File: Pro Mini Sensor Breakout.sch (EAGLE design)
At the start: 15 parts, among them J1 22-27-2021-02, J10 22-27-2021-02, J11 22-27-2021-02, J12 22-27-2021-02, J2 22-27-2041-04, J3 22-27-2041-04, J4 22-27-2031-03, J5 22-27-2041-04, J6 22-27-2041-04, J7 22-27-2031-03, J8 22-27-2021-02, J9 22-27-2021-02, U1 ARDUINO_PRO_MINI

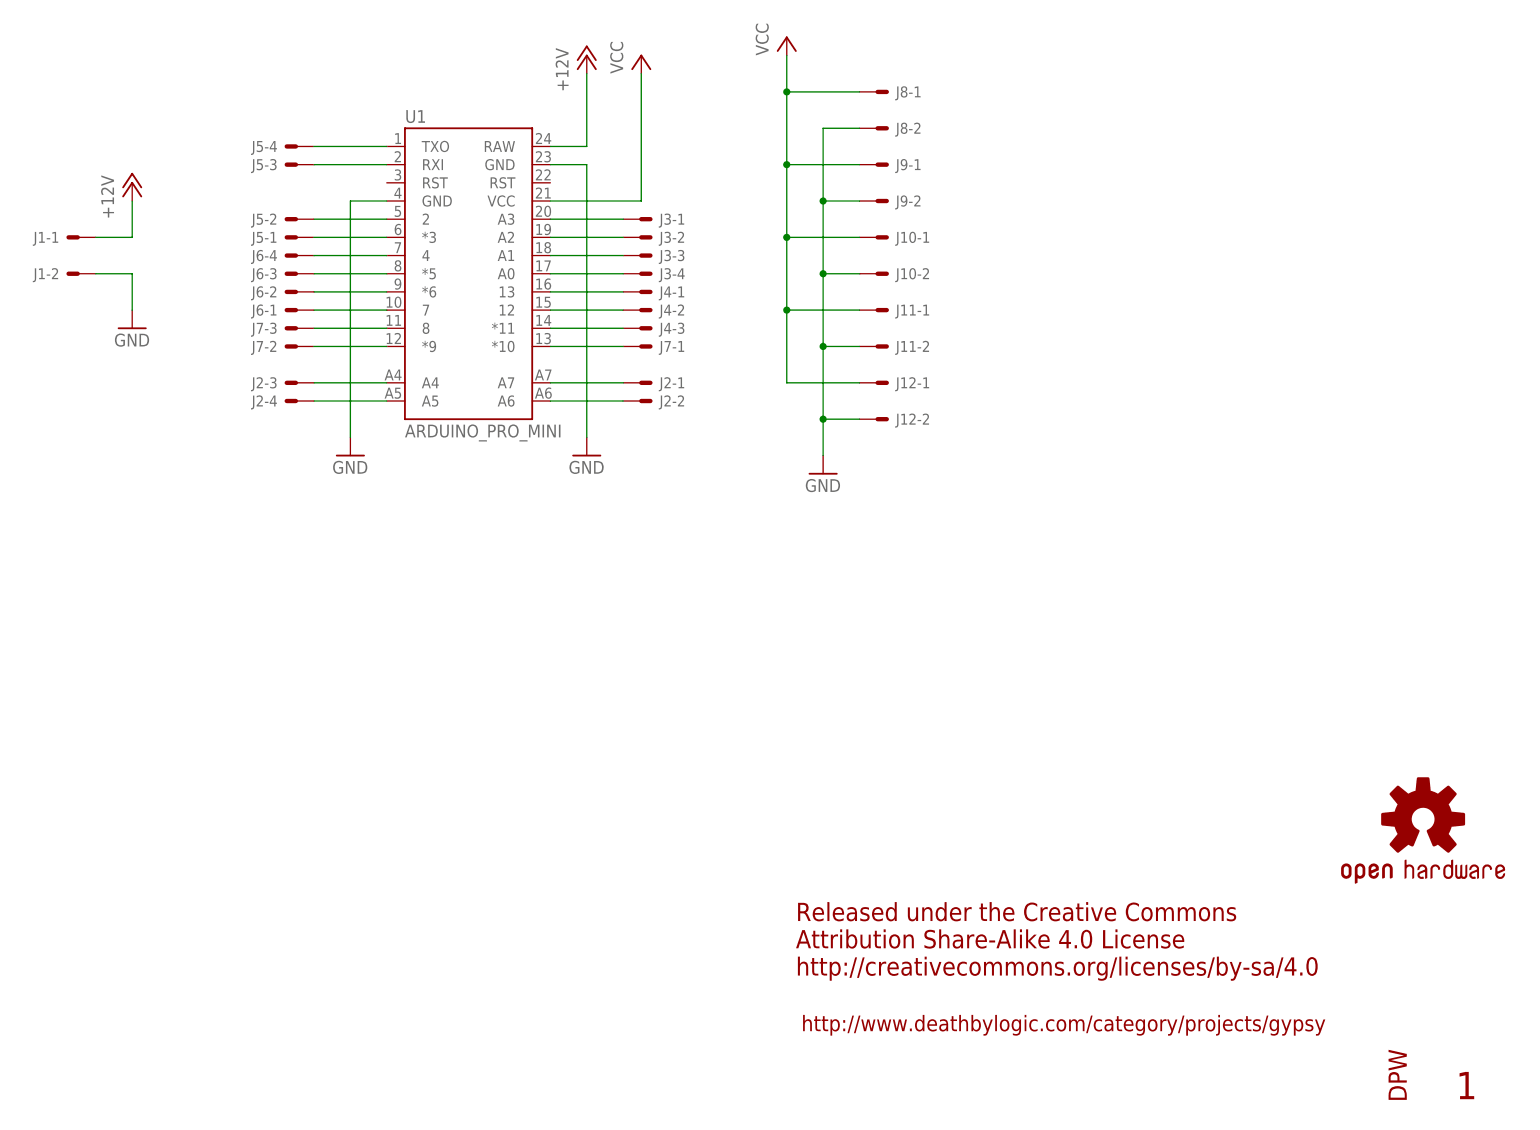
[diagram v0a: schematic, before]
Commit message: Corrected mis-wire of A4 & A5.
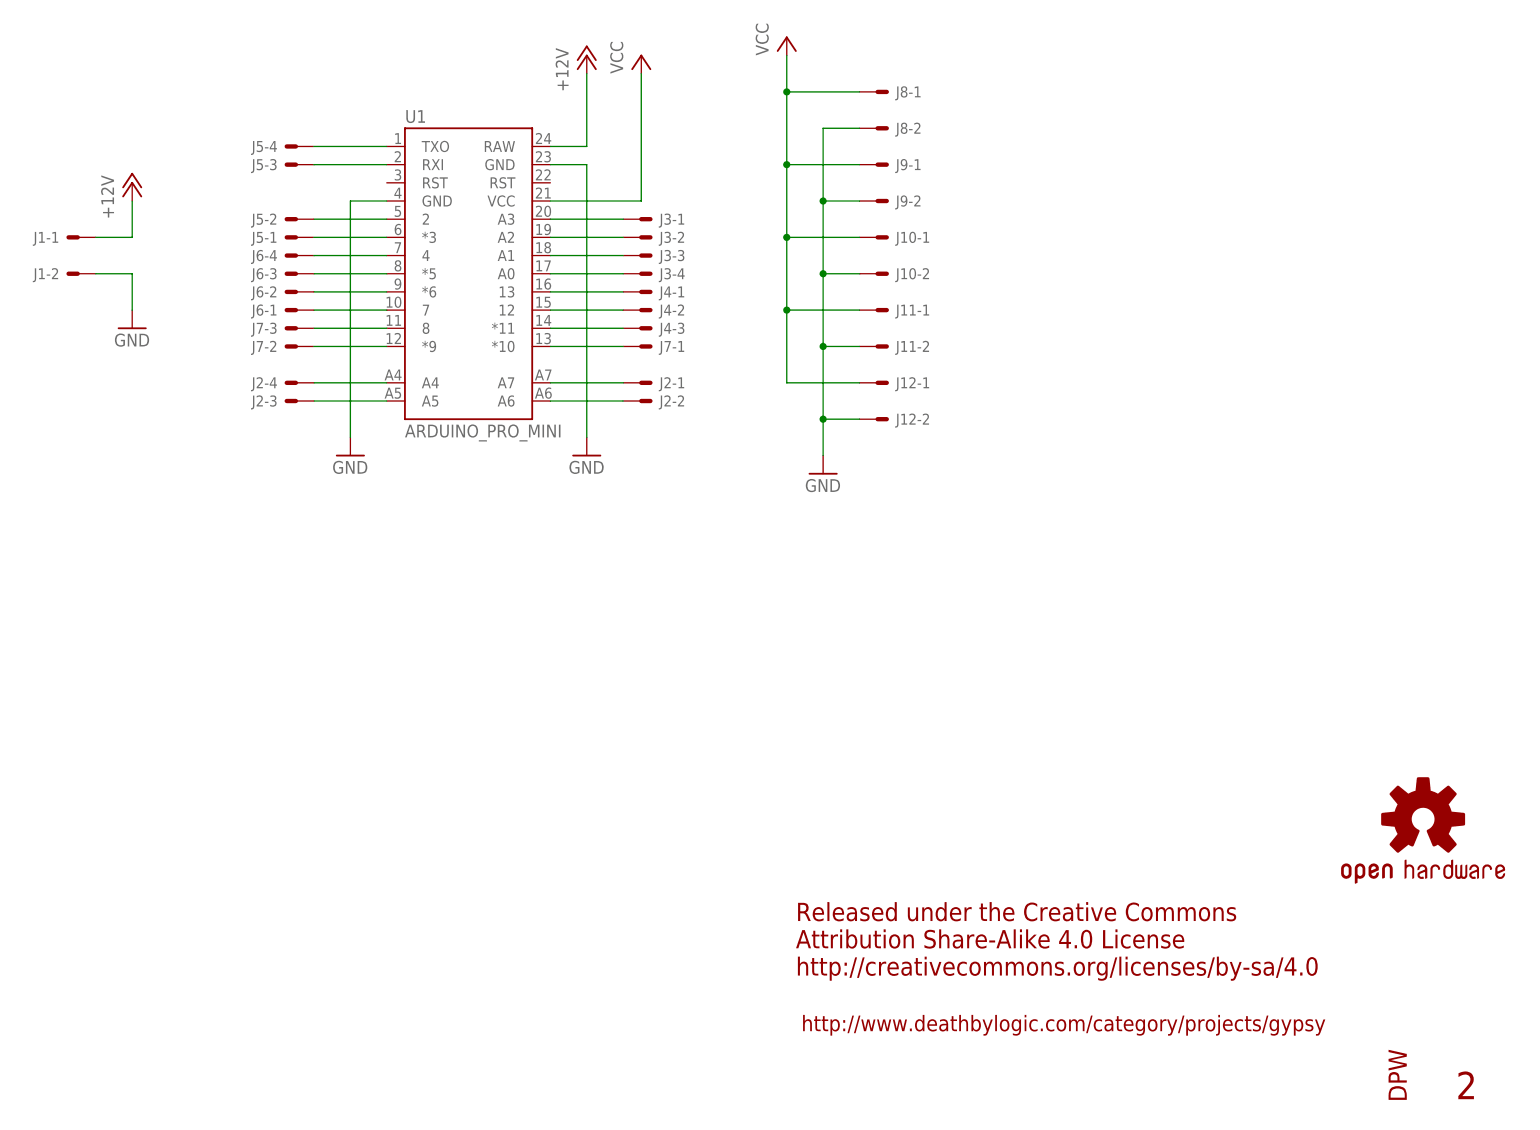
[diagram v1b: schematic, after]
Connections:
- removed net N$3: J2-4.S, U1.A5
- new net N$1: J2-4.S, U1.A4
- net N$2: now also U1.A5; no longer U1.A4
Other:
- note added: "2"
- note removed: "1"
- moved on the sheet: J2-3, J2-4
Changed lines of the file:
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@@
 <setting verticaltext="up"/>
 </settings>
-<grid distance="0.1" unitdist="inch" unit="inch" style="dots" multiple="1" display="yes" altdistance="0.01" altunitdist="inch" altunit="inch"/>
+<grid distance="0.1" unitdist="inch" unit="inch" style="lines" multiple="1" display="no" altdistance="0.01" altunitdist="inch" altunit="inch"/>
 <layers>
 <layer number="1" name="Top" color="4" fill="1" visible="no" active="no"/>
@@
 Attribution Share-Alike 4.0 License
 http://creativecommons.org/licenses/by-sa/4.0</text>
-<text x="266.192" y="6.604" size="3.81" layer="94" font="vector">1</text>
+<text x="266.192" y="6.604" size="3.81" layer="94" font="vector">2</text>
 </plain>
 <instances>
@@
 </instance>
 <instance part="J2" gate="-2" x="152.4" y="104.14"/>
-<instance part="J2" gate="-3" x="104.14" y="106.68" rot="MR0"/>
-<instance part="J2" gate="-4" x="104.14" y="104.14" rot="MR0"/>
+<instance part="J2" gate="-3" x="104.14" y="104.14" rot="MR0"/>
+<instance part="J2" gate="-4" x="104.14" y="106.68" rot="MR0"/>
 <instance part="J3" gate="-1" x="152.4" y="129.54" smashed="yes">
 <attribute name="NAME" x="154.94" y="128.778" size="1.524" layer="95"/>
@@
 </segment>
 </net>
-<net name="N$2" class="0">
-<segment>
-<pinref part="J2" gate="-3" pin="S"/>
-<pinref part="U1" gate="G$1" pin="A4"/>
-<wire x1="106.68" y1="106.68" x2="116.84" y2="106.68" width="0.1524" layer="91"/>
-</segment>
-</net>
-<net name="N$3" class="0">
-<segment>
-<pinref part="U1" gate="G$1" pin="A5"/>
-<pinref part="J2" gate="-4" pin="S"/>
-<wire x1="116.84" y1="104.14" x2="106.68" y2="104.14" width="0.1524" layer="91"/>
-</segment>
-</net>
 <net name="N$4" class="0">
 <segment>
@@
 </segment>
 </net>
+<net name="N$1" class="0">
+<segment>
+<pinref part="J2" gate="-4" pin="S"/>
+<pinref part="U1" gate="G$1" pin="A4"/>
+<wire x1="106.68" y1="106.68" x2="116.84" y2="106.68" width="0.1524" layer="91"/>
+</segment>
+</net>
+<net name="N$2" class="0">
+<segment>
+<pinref part="U1" gate="G$1" pin="A5"/>
+<pinref part="J2" gate="-3" pin="S"/>
+<wire x1="116.84" y1="104.14" x2="106.68" y2="104.14" width="0.1524" layer="91"/>
+</segment>
+</net>
